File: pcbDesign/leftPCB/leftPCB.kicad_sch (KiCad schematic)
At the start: 11 parts, among them J1 Conn_01x12_Pin, SW1 UP, SW2 DOWN, SW3 LEFT, SW4 RIGHT

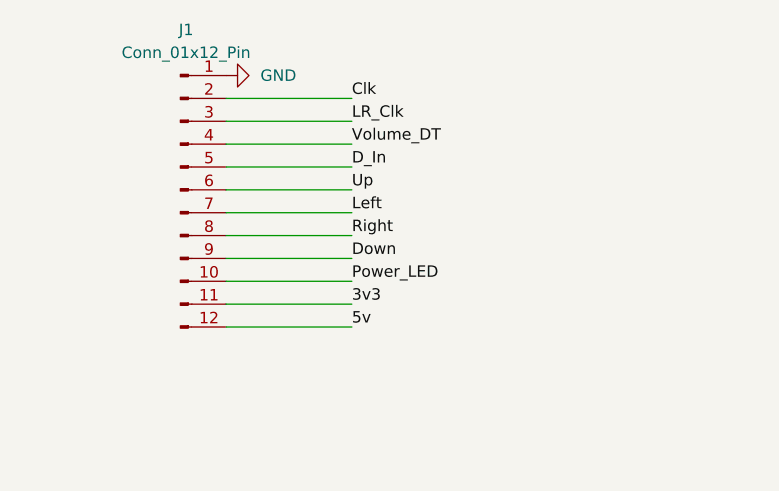
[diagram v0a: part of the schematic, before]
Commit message: Updated left header pins
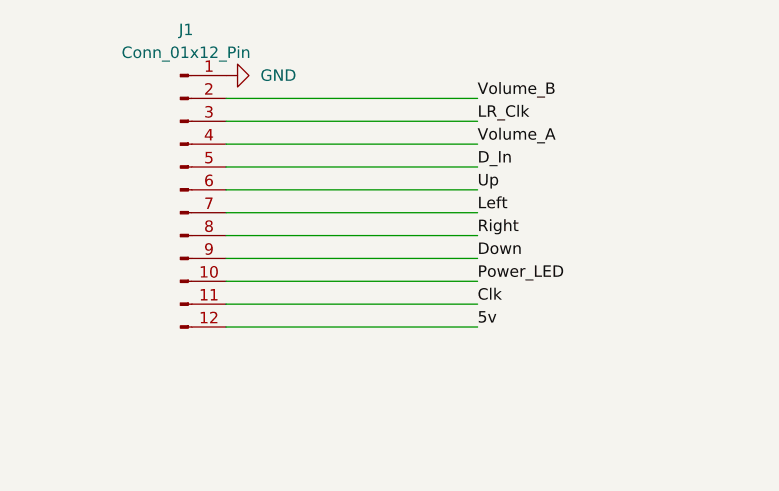
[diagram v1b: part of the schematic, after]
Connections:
- net 3v3 is gone; now on net Clk: J1.11 (Pin_11)
- net Clk: no longer J1.2 (Pin_2)
- net Volume_DT renamed Volume_A
- new net Volume_B: J1.2 (Pin_2)
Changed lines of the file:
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@@
 (kicad_sch
-	(version 20231120)
+	(version 20250114)
 	(generator "eeschema")
-	(generator_version "8.0")
+	(generator_version "9.0")
 	(paper "A4")
 	(junction
@@
 	(wire
 		(pts
-			(xy 127 67.31) (xy 140.97 67.31)
+			(xy 127 67.31) (xy 154.94 67.31)
 		)
 		(stroke
@@
 	(wire
 		(pts
-			(xy 127 49.53) (xy 140.97 49.53)
+			(xy 127 49.53) (xy 154.94 49.53)
 		)
 		(stroke
@@
 	(wire
 		(pts
-			(xy 127 62.23) (xy 140.97 62.23)
+			(xy 127 62.23) (xy 154.94 62.23)
 		)
 		(stroke
@@
 	(wire
 		(pts
-			(xy 127 57.15) (xy 140.97 57.15)
+			(xy 127 57.15) (xy 154.94 57.15)
 		)
 		(stroke
@@
 	(wire
 		(pts
-			(xy 127 54.61) (xy 140.97 54.61)
+			(xy 127 54.61) (xy 154.94 54.61)
 		)
 		(stroke
@@
 	(wire
 		(pts
-			(xy 127 52.07) (xy 140.97 52.07)
-		)
-		(stroke
-			(width 0)
-			(type default)
-		)
-	)
-	(wire
-		(pts
-			(xy 127 46.99) (xy 140.97 46.99)
+			(xy 127 52.07) (xy 154.94 52.07)
+		)
+		(stroke
+			(width 0)
+			(type default)
+		)
+	)
+	(wire
+		(pts
+			(xy 127 46.99) (xy 154.94 46.99)
 		)
 		(stroke
@@
 	(wire
 		(pts
-			(xy 127 41.91) (xy 140.97 41.91)
+			(xy 127 41.91) (xy 154.94 41.91)
 		)
 		(stroke
@@
 	(wire
 		(pts
-			(xy 127 59.69) (xy 140.97 59.69)
-		)
-		(stroke
-			(width 0)
-			(type default)
-		)
-	)
-	(wire
-		(pts
-			(xy 127 44.45) (xy 140.97 44.45)
-		)
-		(stroke
-			(width 0)
-			(type default)
-		)
-	)
-	(wire
-		(pts
-			(xy 127 64.77) (xy 140.97 64.77)
+			(xy 127 59.69) (xy 154.94 59.69)
+		)
+		(stroke
+			(width 0)
+			(type default)
+		)
+	)
+	(wire
+		(pts
+			(xy 127 44.45) (xy 154.94 44.45)
+		)
+		(stroke
+			(width 0)
+			(type default)
+		)
+	)
+	(wire
+		(pts
+			(xy 127 64.77) (xy 154.94 64.77)
 		)
 		(stroke
@@
 	(label "Power_LED"
 		(at 148.59 97.79 0)
-		(fields_autoplaced yes)
 		(effects
 			(font
@@
 		)
 	)
-	(label "3v3"
-		(at 140.97 64.77 0)
-		(fields_autoplaced yes)
+	(label "Down"
+		(at 154.94 59.69 0)
 		(effects
 			(font
@@
 		)
 	)
-	(label "Power_LED"
-		(at 140.97 62.23 0)
-		(fields_autoplaced yes)
+	(label "Volume_B"
+		(at 154.94 41.91 0)
 		(effects
 			(font
@@
 		)
 	)
-	(label "Clk"
-		(at 140.97 41.91 0)
-		(fields_autoplaced yes)
+	(label "D_In"
+		(at 154.94 49.53 0)
 		(effects
 			(font
@@
 		)
 	)
-	(label "Down"
-		(at 140.97 59.69 0)
-		(fields_autoplaced yes)
+	(label "Power_LED"
+		(at 154.94 62.23 0)
 		(effects
 			(font
@@
 	)
 	(label "Up"
-		(at 140.97 52.07 0)
-		(fields_autoplaced yes)
+		(at 154.94 52.07 0)
 		(effects
 			(font
@@
 		)
 	)
-	(label "Right"
-		(at 71.12 74.93 0)
-		(fields_autoplaced yes)
+	(label "Left"
+		(at 154.94 54.61 0)
 		(effects
 			(font
@@
 		)
 	)
-	(label "Left"
-		(at 140.97 54.61 0)
-		(fields_autoplaced yes)
+	(label "Right"
+		(at 71.12 74.93 0)
 		(effects
 			(font
@@
 		)
 	)
-	(label "5v"
-		(at 140.97 67.31 0)
-		(fields_autoplaced yes)
+	(label "Right"
+		(at 154.94 57.15 0)
 		(effects
 			(font
@@
 		)
 	)
-	(label "Volume_DT"
-		(at 140.97 46.99 0)
-		(fields_autoplaced yes)
+	(label "LR_Clk"
+		(at 154.94 44.45 0)
 		(effects
 			(font
@@
 		)
 	)
-	(label "Right"
-		(at 140.97 57.15 0)
-		(fields_autoplaced yes)
+	(label "Down"
+		(at 71.12 52.07 0)
 		(effects
 			(font
@@
 		)
 	)
-	(label "Down"
-		(at 71.12 52.07 0)
-		(fields_autoplaced yes)
+	(label "Up"
+		(at 71.12 40.64 0)
 		(effects
 			(font
@@
 		)
 	)
-	(label "D_In"
-		(at 140.97 49.53 0)
-		(fields_autoplaced yes)
+	(label "5v"
+		(at 154.94 67.31 0)
 		(effects
 			(font
@@
 		)
 	)
-	(label "Up"
-		(at 71.12 40.64 0)
-		(fields_autoplaced yes)
+	(label "Volume_A"
+		(at 154.94 46.99 0)
 		(effects
 			(font
@@
 	(label "Left"
 		(at 71.12 63.5 0)
-		(fields_autoplaced yes)
 		(effects
 			(font
@@
 		)
 	)
-	(label "LR_Clk"
-		(at 140.97 44.45 0)
-		(fields_autoplaced yes)
+	(label "Clk"
+		(at 154.94 64.77 0)
 		(effects
 			(font
@@
 		)
 	)
+	(embedded_fonts no)
 )

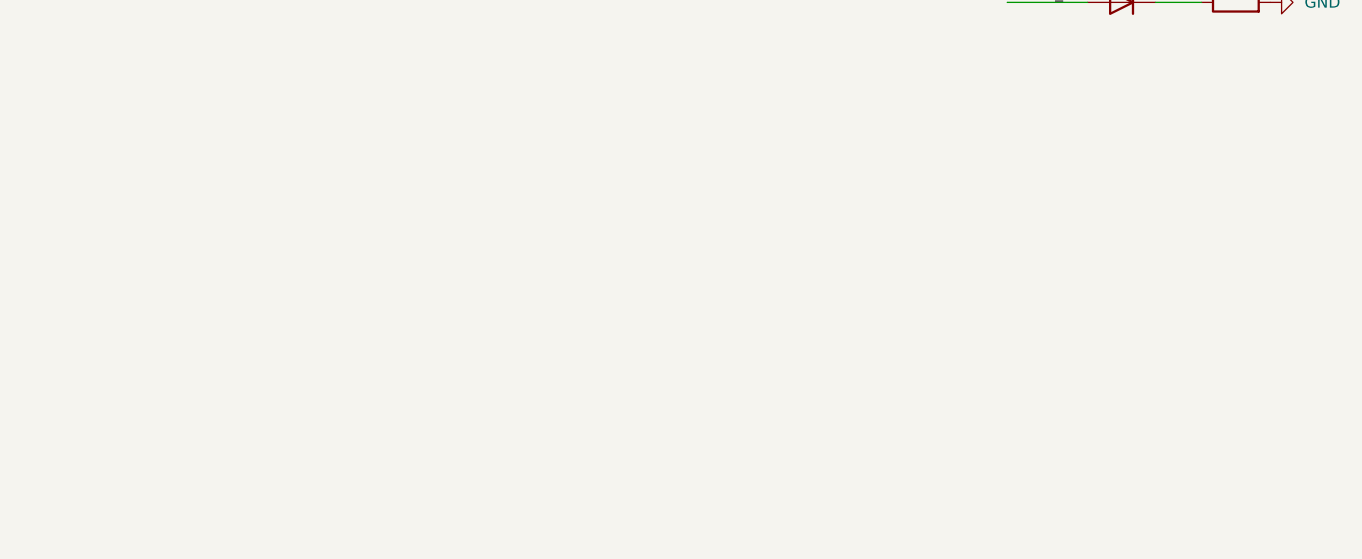
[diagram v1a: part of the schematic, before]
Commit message: Updated PCB designs for left and right boards
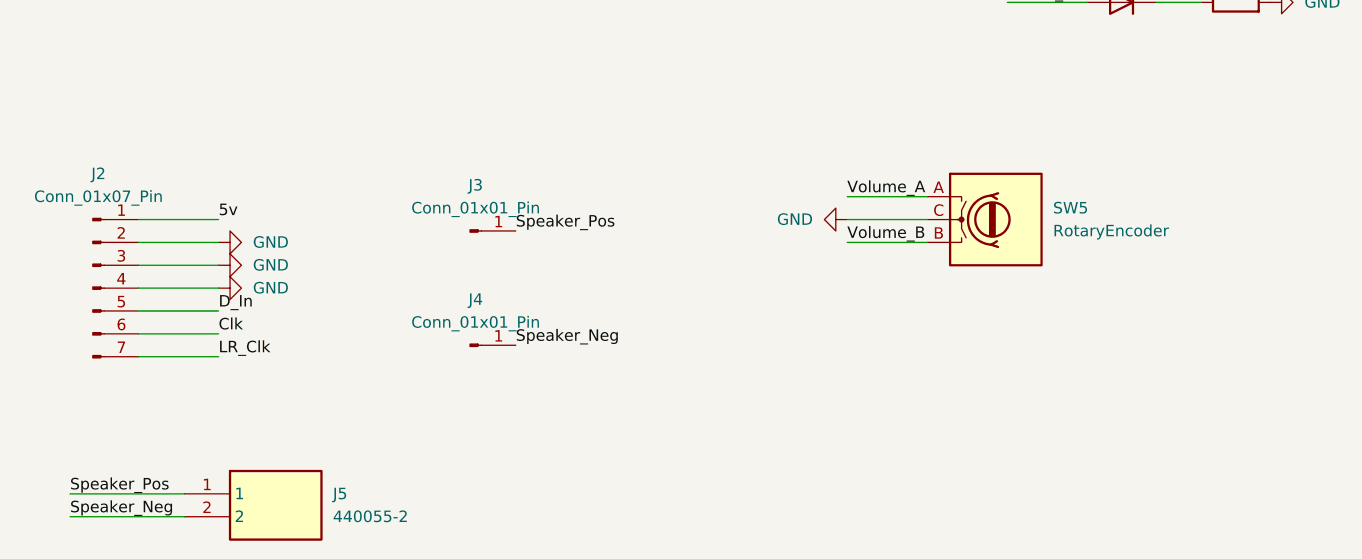
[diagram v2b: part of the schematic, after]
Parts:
- added J2: Conn_01x07_Pin, Connector_PinHeader_2.54mm:PinHeader_1x07_P2.54mm_Vertical, symbol Connector:Conn_01x07_Pin
- added J3, J4: Conn_01x01_Pin, Connector_PinHeader_2.54mm:PinHeader_1x01_P2.54mm_Vertical, symbol Connector:Conn_01x01_Pin
- added J5: 440055-2, SHDRRA2W50P0X200_1X2_600X770X525P, symbol 440055-2:440055-2
- added SW5: RotaryEncoder, GGfoorptintLibrary:PES12, symbol Device:RotaryEncoder
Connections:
- net 5v: now also J2.1 (Pin_1)
- net Clk: now also J2.6 (Pin_6)
- net D_In: now also J2.5 (Pin_5)
- net GND: now also J2.2 (Pin_2), J2.3 (Pin_3), J2.4 (Pin_4), SW5.C
- net LR_Clk: now also J2.7 (Pin_7)
- net Volume_A: now also SW5.A
- net Volume_B: now also SW5.B
- new net Speaker_Neg: J4.1 (Pin_1), J5.2
- new net Speaker_Pos: J3.1 (Pin_1), J5.1

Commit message: Routed
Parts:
- added H1: MountingHole, MountingHole:MountingHole_3.5mm, symbol Mechanical:MountingHole
- added H2, H3, H4, H5, H6: MountingHole, MountingHole:MountingHole_2mm, symbol Mechanical:MountingHole

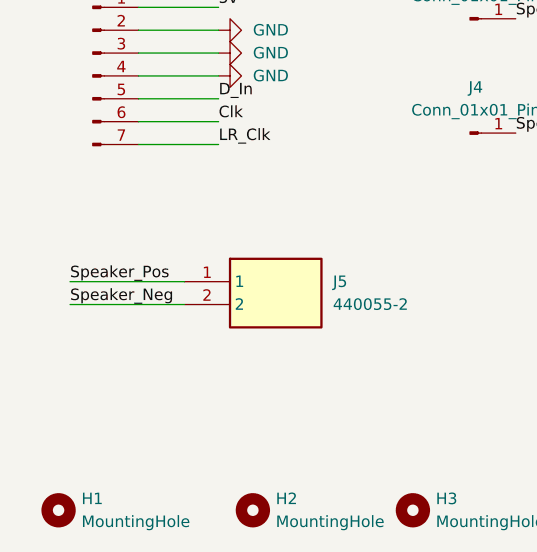
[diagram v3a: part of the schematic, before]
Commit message: Finalized placement on left pcb
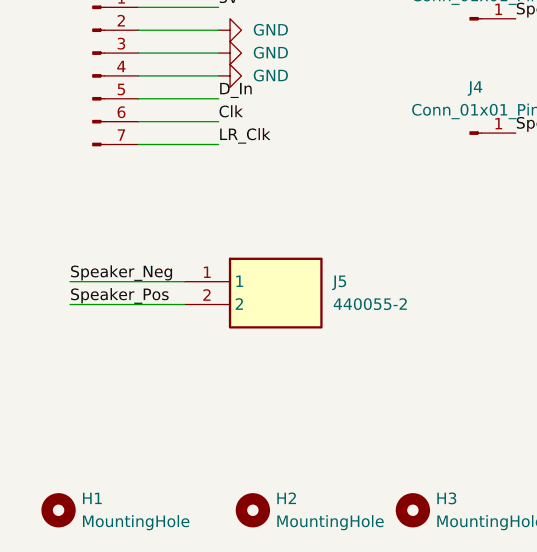
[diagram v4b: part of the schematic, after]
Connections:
- net Speaker_Neg: now also J5.1; no longer J5.2
- net Speaker_Pos: now also J5.2; no longer J5.1
